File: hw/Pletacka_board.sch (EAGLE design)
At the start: 59 parts, among them U1 LM75BDP-NEW, U2 EL357N(A)(TA)-G, U3 EL357N(A)(TA)-G, U4 EL357N(A)(TA)-G, U5 EL357N(A)(TA)-G, U6 TPS54231D

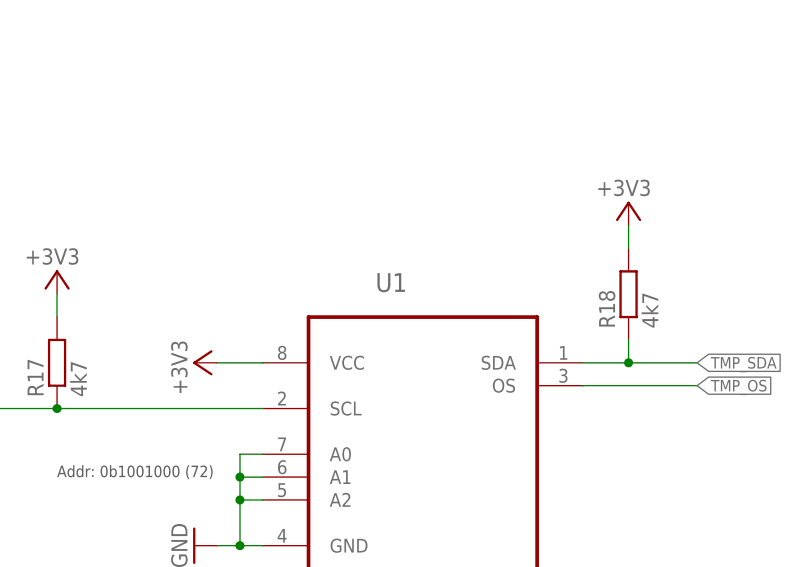
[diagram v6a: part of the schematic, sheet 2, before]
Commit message: Fix ports rotation
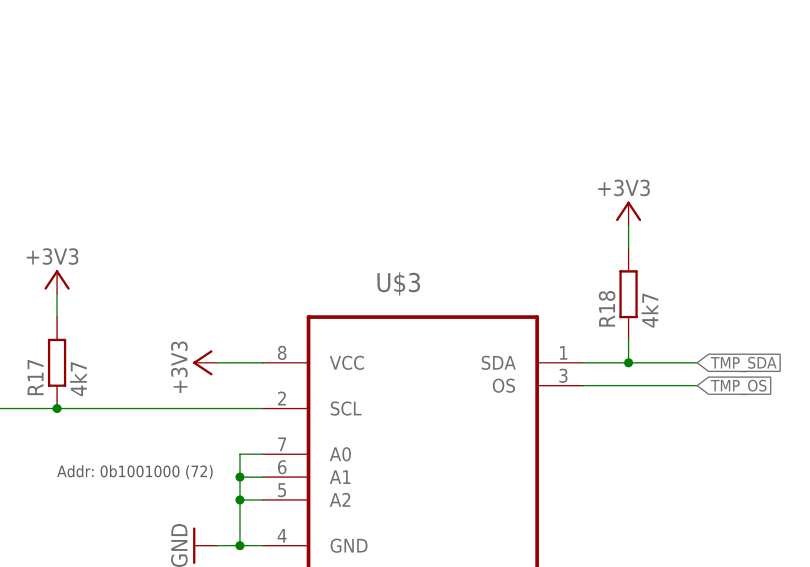
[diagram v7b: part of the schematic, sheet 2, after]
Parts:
- renumbered U1 to U$3
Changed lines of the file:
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@@
 <part name="+3V1" library="supply1" library_urn="urn:adsk.eagle:library:371" deviceset="+3V3" device=""/>
 <part name="P+1" library="supply1" library_urn="urn:adsk.eagle:library:371" deviceset="+5V" device=""/>
-<part name="U1" library="LM75BDP" deviceset="LM75BDP-NEW" device="">
-<attribute name="LCSC_ID" value="C33099"/>
-</part>
 <part name="+3V2" library="supply1" library_urn="urn:adsk.eagle:library:371" deviceset="+3V3" device=""/>
 <part name="GND3" library="supply1" library_urn="urn:adsk.eagle:library:371" deviceset="GND" device=""/>
@@
 </spice>
 <attribute name="LCSC_ID" value="C23147"/>
+</part>
+<part name="U$3" library="LM75BDP" deviceset="LM75BDP-NEW" device="">
+<attribute name="LCSC_ID" value="C33099"/>
 </part>
 </parts>
@@
 <attribute name="SHEET" x="230.505" y="5.08" size="2.54" layer="94"/>
 </instance>
-<instance part="U1" gate="G$1" x="198.12" y="66.04" smashed="yes">
-<attribute name="NAME" x="192.852159375" y="81.5381" size="2.08678125" layer="95" ratio="10" rot="SR0"/>
-<attribute name="VALUE" x="193.74995" y="43.6562" size="2.083390625" layer="96" ratio="10" rot="SR0"/>
-<attribute name="LCSC_ID" x="198.12" y="66.04" size="1.778" layer="96" display="off"/>
-</instance>
 <instance part="+3V2" gate="G$1" x="172.72" y="73.66" smashed="yes" rot="R90">
 <attribute name="VALUE" x="170.18" y="76.2" size="1.778" layer="96" rot="R270"/>
@@
 <instance part="+3V9" gate="G$1" x="220.98" y="91.44" smashed="yes">
 <attribute name="VALUE" x="223.52" y="93.98" size="1.778" layer="96" rot="R180"/>
+</instance>
+<instance part="U$3" gate="G$1" x="198.12" y="66.04" smashed="yes">
+<attribute name="NAME" x="192.852159375" y="81.5381" size="2.08678125" layer="95" ratio="10" rot="SR0"/>
+<attribute name="VALUE" x="193.74995" y="43.6562" size="2.083390625" layer="96" ratio="10" rot="SR0"/>
+<attribute name="LCSC_ID" x="198.12" y="66.04" size="1.778" layer="96" display="off"/>
 </instance>
 </instances>
@@
 <net name="GND" class="0">
 <segment>
-<pinref part="U1" gate="G$1" pin="GND"/>
 <wire x1="180.34" y1="53.34" x2="177.8" y2="53.34" width="0.1524" layer="91"/>
 <pinref part="GND3" gate="1" pin="GND"/>
-<pinref part="U1" gate="G$1" pin="A0"/>
 <wire x1="177.8" y1="53.34" x2="175.26" y2="53.34" width="0.1524" layer="91"/>
 <wire x1="180.34" y1="63.5" x2="177.8" y2="63.5" width="0.1524" layer="91"/>
 <wire x1="177.8" y1="63.5" x2="177.8" y2="60.96" width="0.1524" layer="91"/>
-<pinref part="U1" gate="G$1" pin="A1"/>
 <wire x1="177.8" y1="60.96" x2="180.34" y2="60.96" width="0.1524" layer="91"/>
 <wire x1="177.8" y1="60.96" x2="177.8" y2="58.42" width="0.1524" layer="91"/>
 <junction x="177.8" y="60.96"/>
-<pinref part="U1" gate="G$1" pin="A2"/>
 <wire x1="177.8" y1="58.42" x2="180.34" y2="58.42" width="0.1524" layer="91"/>
 <wire x1="177.8" y1="58.42" x2="177.8" y2="53.34" width="0.1524" layer="91"/>
 <junction x="177.8" y="58.42"/>
 <junction x="177.8" y="53.34"/>
+<pinref part="U$3" gate="G$1" pin="A0"/>
+<pinref part="U$3" gate="G$1" pin="A1"/>
+<pinref part="U$3" gate="G$1" pin="A2"/>
+<pinref part="U$3" gate="G$1" pin="GND"/>
 </segment>
 <segment>
@@
 <net name="TMP_SDA" class="0">
 <segment>
-<pinref part="U1" gate="G$1" pin="SDA"/>
 <wire x1="215.9" y1="73.66" x2="220.98" y2="73.66" width="0.1524" layer="91"/>
 <label x="228.6" y="73.66" size="1.27" layer="95" xref="yes"/>
@@
 <wire x1="220.98" y1="76.2" x2="220.98" y2="73.66" width="0.1524" layer="91"/>
 <junction x="220.98" y="73.66"/>
+<pinref part="U$3" gate="G$1" pin="SDA"/>
 </segment>
 </net>
@@
 <pinref part="R17" gate="G$1" pin="1"/>
 <wire x1="157.48" y1="68.58" x2="147.32" y2="68.58" width="0.1524" layer="91"/>
-<pinref part="U1" gate="G$1" pin="SCL"/>
 <wire x1="157.48" y1="68.58" x2="180.34" y2="68.58" width="0.1524" layer="91"/>
 <junction x="157.48" y="68.58"/>
+<pinref part="U$3" gate="G$1" pin="SCL"/>
 </segment>
 </net>
 <net name="+3V3" class="0">
 <segment>
-<pinref part="U1" gate="G$1" pin="VCC"/>
 <wire x1="180.34" y1="73.66" x2="175.26" y2="73.66" width="0.1524" layer="91"/>
 <pinref part="+3V2" gate="G$1" pin="+3V3"/>
+<pinref part="U$3" gate="G$1" pin="VCC"/>
 </segment>
 <segment>
@@
 <net name="TMP_OS" class="0">
 <segment>
-<pinref part="U1" gate="G$1" pin="OS"/>
 <wire x1="215.9" y1="71.12" x2="228.6" y2="71.12" width="0.1524" layer="91"/>
 <label x="228.6" y="71.12" size="1.27" layer="95" xref="yes"/>
-</segment>
-</net>
+<pinref part="U$3" gate="G$1" pin="OS"/>
+</segment>
+</net>
